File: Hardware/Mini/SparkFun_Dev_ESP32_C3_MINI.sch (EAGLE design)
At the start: 50 parts, among them J1 USB Female Type C Connector, J4 QWIIC_RIGHT_ANGLE, U1 ESP32-C3, U2 RT9080-33GJ5, Y1 40MHZ

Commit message: Adds MINI module, creates new design with MINI module netted
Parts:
- removed C3, C4: 9.1pF, SparkFun-Capacitors:9.1PF-0402-TIGHT
- removed C6: 0.1uF, SparkFun-Capacitors:0.1UF-0402T-6.3V-10%-X7R
- removed C7: 0.1uF, SparkFun-Capacitors:0.1UF-0402T-16V-10%
- removed E1: WIFI_CHIP_ANT, ESP32-C3-MINI-1:WIFI_CHIP_ANT
- removed J4: QWIIC_RIGHT_ANGLE, SparkFun-Connectors:QWIIC_CONNECTORJS-1MM
- removed R8: 100k, SparkFun-Resistors:100KOHM-0402T-1/16W-1%
- removed U1: ESP32-C3, ESP32-C3-MINI-1:ESP32-C3
- removed Y1: 40MHZ, SparkFun-Clocks:CRYSTAL-40MHZ-SMD-2X2.5MM
- added J5: Vertical Qwiic Connector, SparkFun-Connectors:QWIIC_CONNECTOR
- added U$1: ESP32-C3_MINI-1, ESP32-C3-MINI-1:ESP32-C3_MINI-1
- C9: value 10nF -> 10uF; device SparkFun-Capacitors:10NF-0402T-25V-10% -> SparkFun-Capacitors:10UF-0402T-6.3V-20%
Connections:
- removed net ANT: E1.SIGNAL, U1.LNA_IN
- removed net IO0/A0: J3.8, U1.XTAL_32K_P/IO0
- removed net IO1/A1: J3.7, U1.XTAL_32K_N/IO1
- removed net IO12: J2.5, U1.SPIHD/IO12
- removed net IO13/SDA: J2.8, J4.3, R3.1, U1.SPIWP/IO13
- removed net IO14/SCL: J2.7, J4.4, R4.2, U1.SPICS0/IO14
- removed net IO15: J2.4, U1.SPICLK/IO15
- removed net IO16: J2.3, U1.SPID/IO16
- removed net IO17: U1.SPIQ/IO17
- removed net IO2/POCI: J3.10, R9.1, U1.FSPIQ/IO2
- removed net IO3/A3: J3.6, U1.IO3
- removed net IO4/A4/MTMS: J3.5, TP4.1, U1.MTMS/FSPIHD/IO4
- removed net IO5/A5/MTDI: J3.12, TP6.1, U1.MTDI/FSPIWP/IO5
- removed net IO6/SCLK/MTCK: J3.9, TP3.1, U1.MTCK/FSPICLK/IO6
- removed net IO7/PICO/MTDO: J3.11, TP1.1, U1.MTDO/FSPID/IO7
- removed net N$10: C4.2, U1.XTAL_P, Y1.2
- removed net N$6: R8.2, U2.EN
- removed net N$9: C3.2, U1.XTAL_N, Y1.1
- removed net NC: J2.1, J2.2
- new net IO5/SCL: J2.8, J5.4, R4.2, TP6.1, U$1.IO5
- new net IO6/SDA: J2.7, J5.3, R3.1, TP3.1, U$1.IO6
- new net IO7/STAT: J2.6, STAT.2, TP1.1, U$1.IO7
- new net IOA0/SCLK: J3.7, U$1.IOA0
- new net IOA1/POCI: J3.6, U$1.IOA1
- new net IOA2: J3.9, R9.1, U$1.IOA2
- new net IOA3/PICO: J3.5, TP4.1, U$1.IOA3
- new net IOA4: J3.8, U$1.IOA4
- net 3.3V: now also J5.2, U$1.3V3; no longer C7.1, J4.2, STAT.2, U1.VDD3P3, U1.VDD3P3_CPU, U1.VDD3P3_RTC, U1.VDDA
- net EN: now also U$1.EN; no longer U1.CHIP_EN
- net GND: now also J5.1, U$1.GND; no longer C3.1, C4.1, C6.2, C7.2, E1.GND, J4.1, U1.GND, Y1.GND
- net IO10: now also J2.4, U$1.IO10; no longer J2.6, U1.FSPICS0/IO10
- net IO18/USB_N: now also U$1.USB_D-/IO18; no longer U1.USB_D-/IO18
- net IO19/USB_P: now also U$1.USB_D+/IO19; no longer U1.USB_D+/IO19
- net IO20/TXO: now also U$1.RXD/IO20; no longer U1.RXD/IO20
- net IO21/RXI: now also U$1.TXD/IO21; no longer U1.TXD/IO21
- net IO8: now also J2.5, U$1.IO8; no longer U1.IO8
- net IO9/BOOT: now also U$1.IO9; no longer C6.1, U1.IO9
- net V_USB: now also U2.EN; no longer R8.1
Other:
- note added: "Digital Decoupling Pins 3"
- note added: "WiFi Module - ESP32-C3 MINI-1"
- note removed: "Analog Decoupling Pins 31,32"
- note removed: "Antenna Space"
- note removed: "Digital Decoupling Pin 17"
- note removed: "WiFi SOC - ESP32-C3"
- moved on the sheet: BOOT, C1, C5, C8, C9, R11, R7, R9, RESET

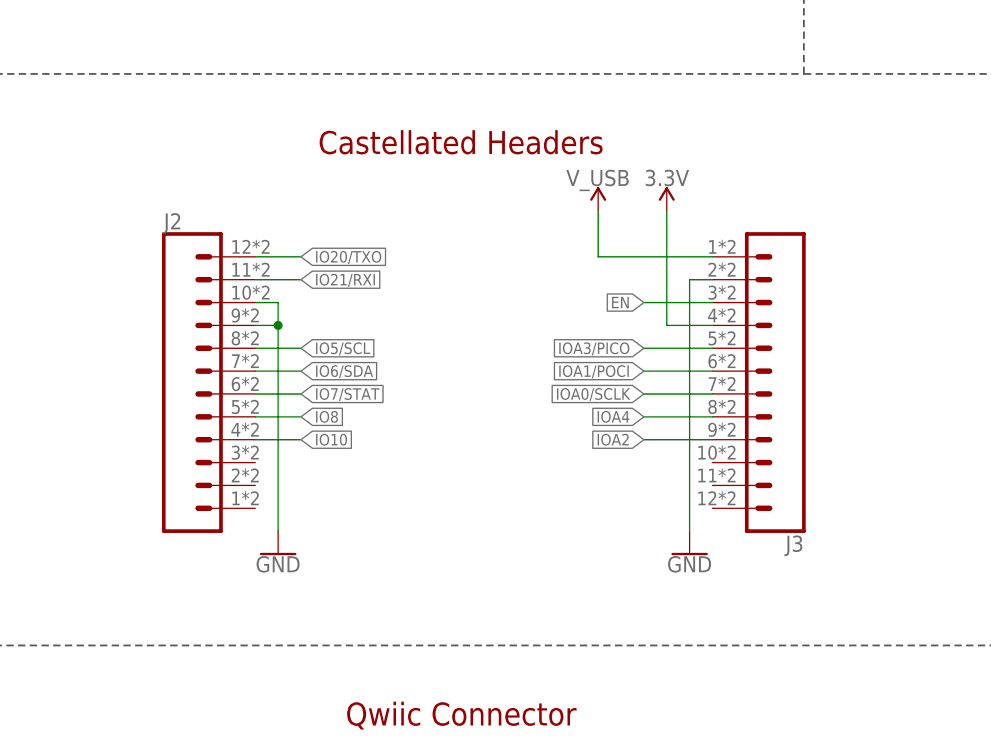
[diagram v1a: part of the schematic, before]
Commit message: Adds 9 pin connector to the MINI designs
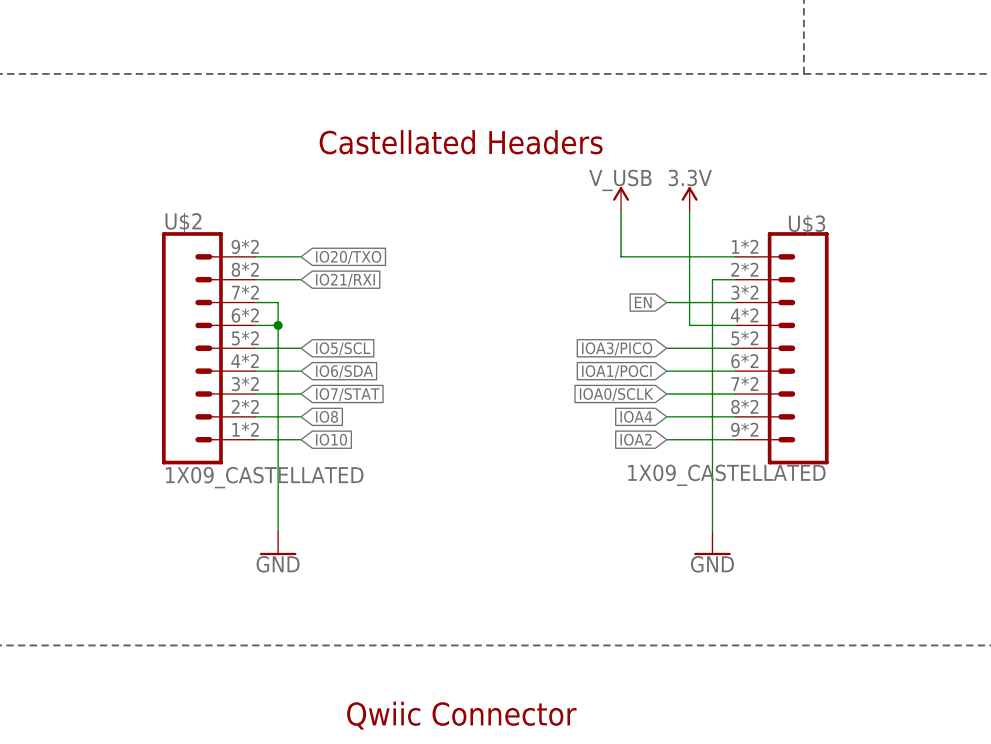
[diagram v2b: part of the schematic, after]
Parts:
- removed J2, J3: (no value), SparkFun-Connectors:CONN_12CASTELLATED
- added U$2, U$3: 1X09_CASTELLATED, ESP32-C3-MINI-1:1X09_CASTELLATED
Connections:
- net 3.3V: now also U$3.4; no longer J3.4
- net EN: now also U$3.3; no longer J3.3
- net GND: now also U$2.6, U$2.7, U$3.2; no longer J2.10, J2.9, J3.2
- net IO10: now also U$2.1; no longer J2.4
- net IO20/TXO: now also U$2.9; no longer J2.12
- net IO21/RXI: now also U$2.8; no longer J2.11
- net IO5/SCL: now also U$2.5; no longer J2.8
- net IO6/SDA: now also U$2.4; no longer J2.7
- net IO7/STAT: now also U$2.3; no longer J2.6
- net IO8: now also U$2.2; no longer J2.5
- net IOA0/SCLK: now also U$3.7; no longer J3.7
- net IOA1/POCI: now also U$3.6; no longer J3.6
- net IOA2: now also U$3.9; no longer J3.9
- net IOA3/PICO: now also U$3.5; no longer J3.5
- net IOA4: now also U$3.8; no longer J3.8
- net V_USB: now also U$3.1; no longer J3.1
